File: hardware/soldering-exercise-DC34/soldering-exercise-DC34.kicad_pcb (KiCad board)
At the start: 2 copper layers, 50 x 50 mm, 30 parts, among them U1 NE555P

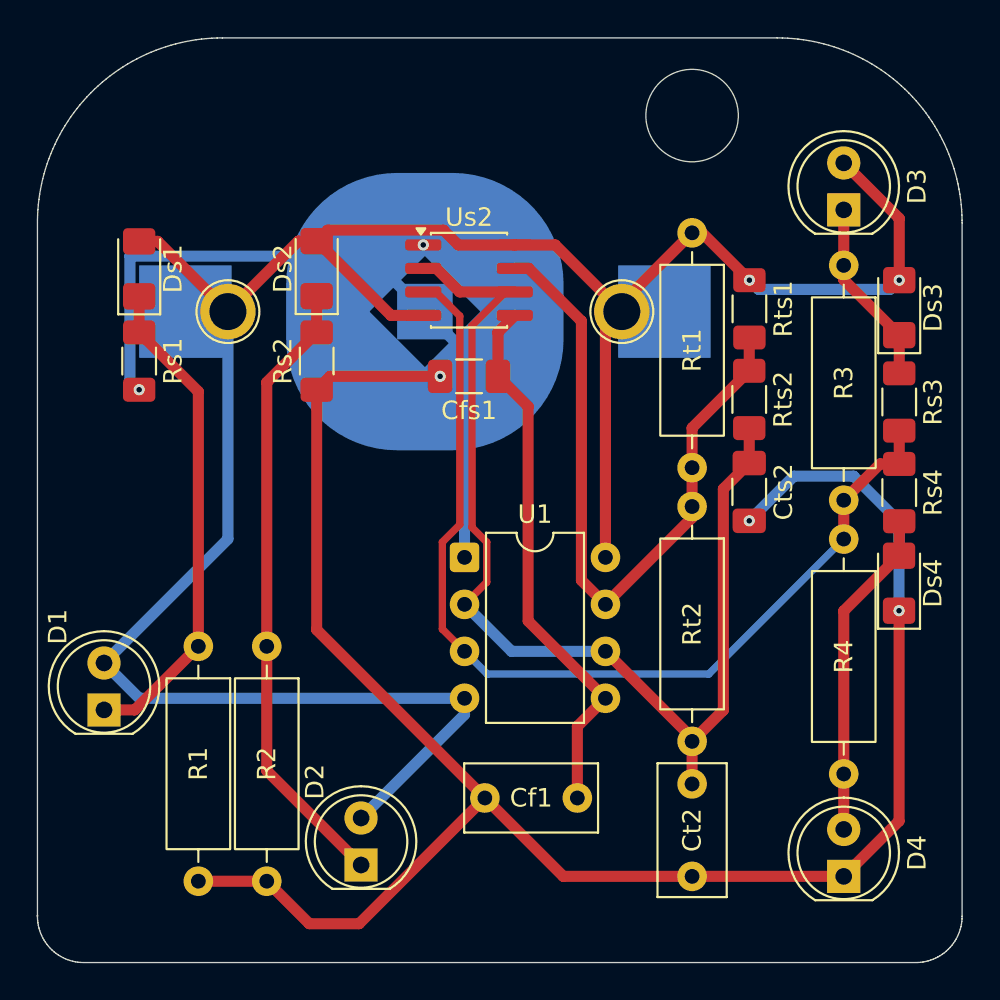
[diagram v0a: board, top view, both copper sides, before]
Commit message: add labs logo
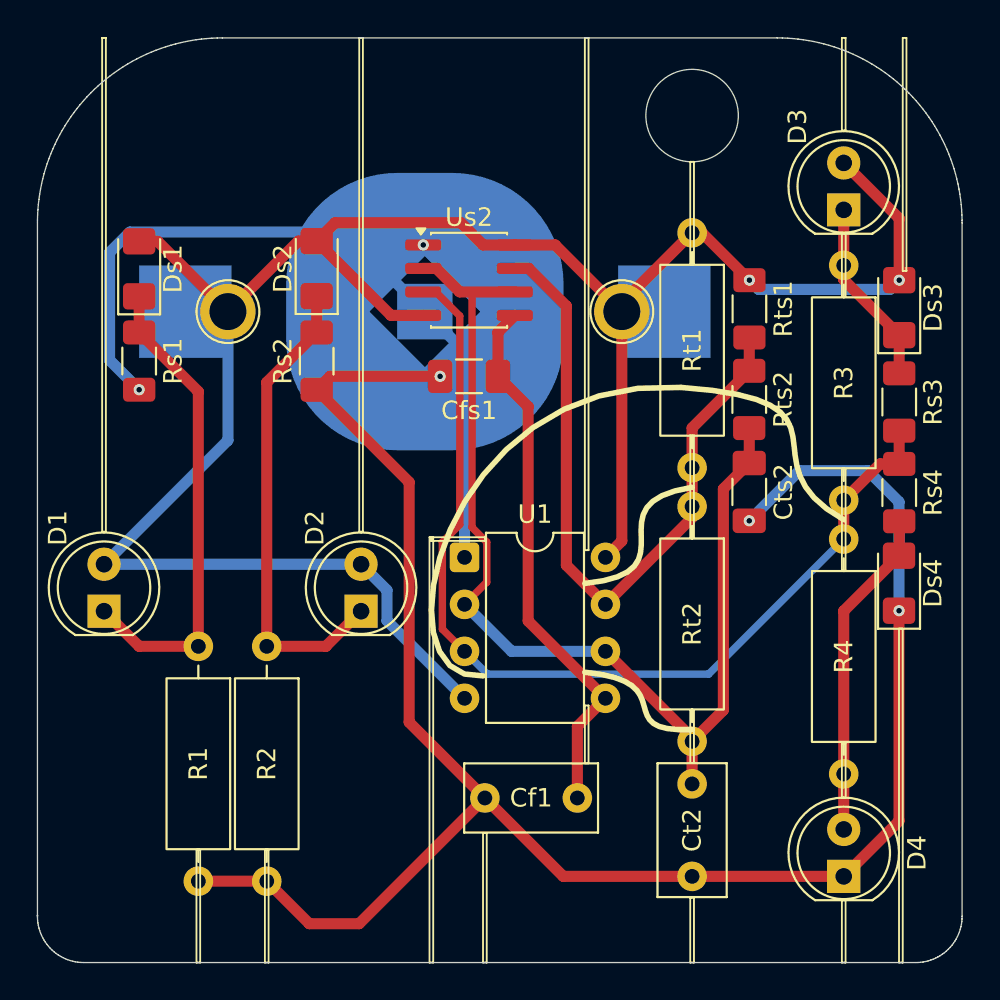
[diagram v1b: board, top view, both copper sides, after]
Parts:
- moved D2 13.7 mm to (92.5, 111.0)
- moved D1 5.34 mm to (78.6, 111.0)
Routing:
- net +V: track 130.0 -> 119.4 mm
- net Net-(D2-K): track 34.0 -> 25.9 mm
- net GND: track 142.6 -> 146.2 mm
- net /THR: track 60.4 -> 61.5 mm
- net Net-(D1-K): track 26.8 -> 26.1 mm
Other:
- board text added: "615-Labs.com"
